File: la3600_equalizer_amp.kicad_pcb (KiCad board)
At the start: 2 copper layers, 95 x 198.6 mm, 54 parts, among them J1 JACK_TRS_3PINS, J2 JACK_TRS_3PINS, J3 USB_B, U1 LA3600, U2 LA3600, U3 LM386, U4 LM386

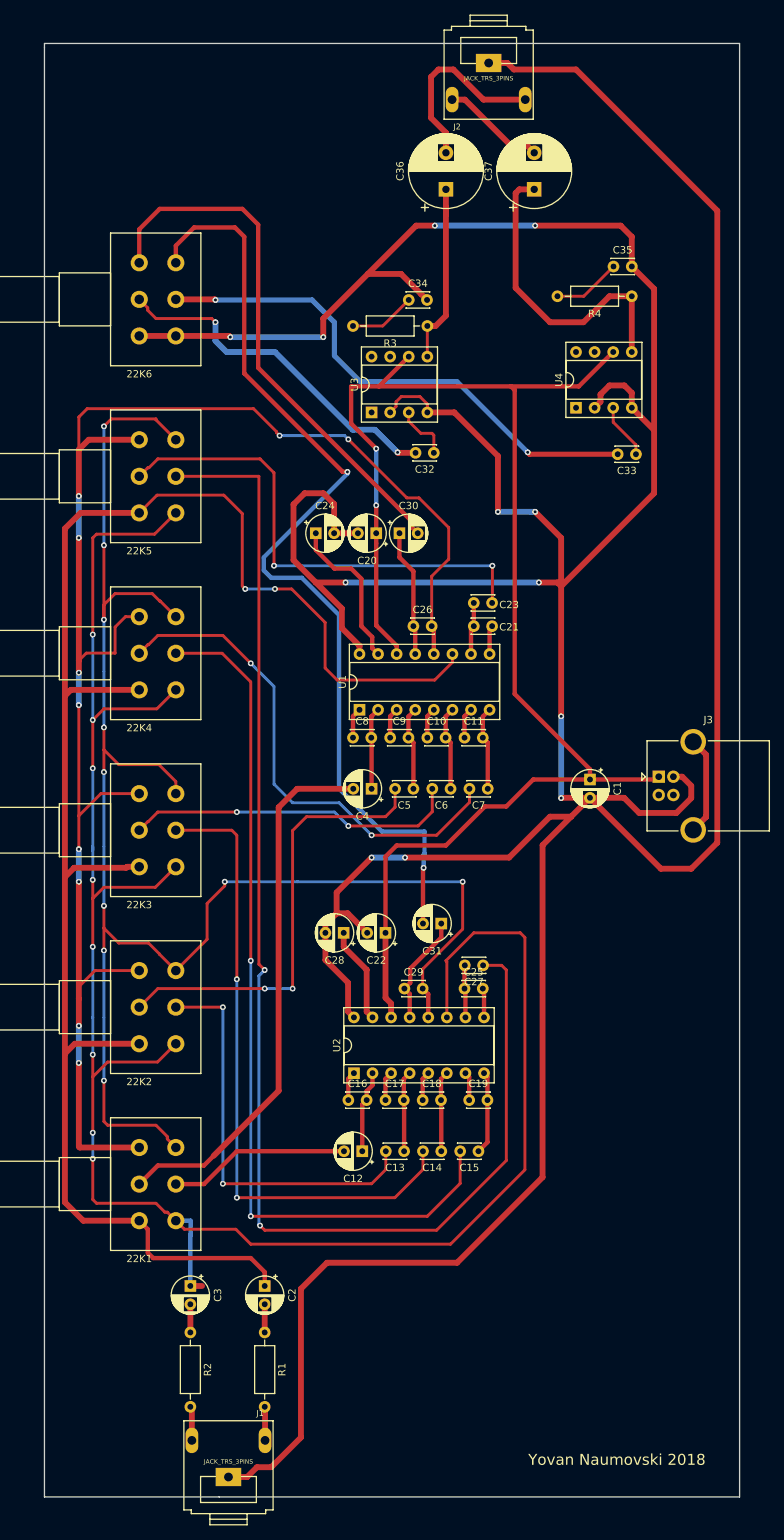
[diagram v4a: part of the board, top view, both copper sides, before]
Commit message: replace the audio amplifier part of the circuit with a new one based on NE5532 and BD139/BD140 output stage
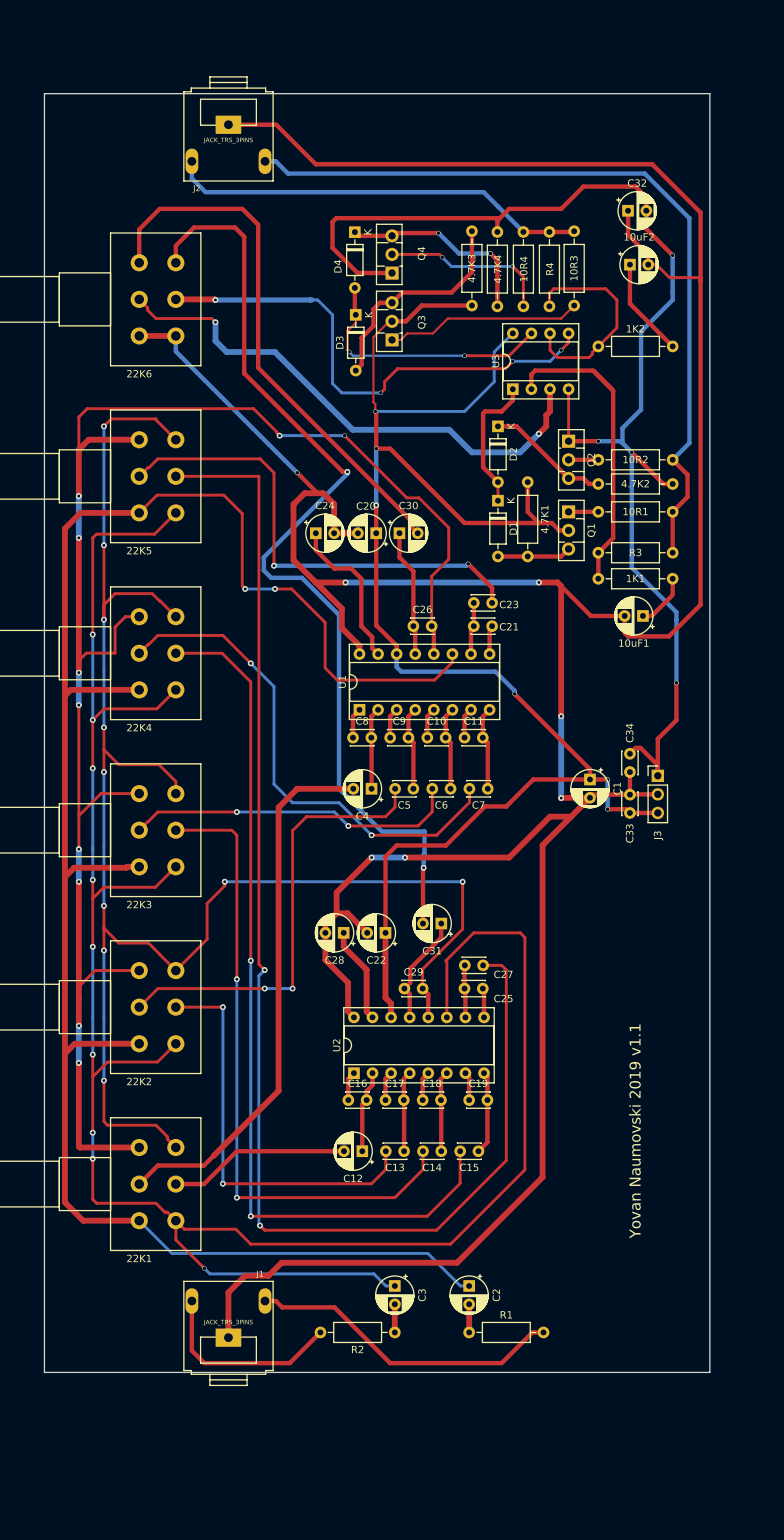
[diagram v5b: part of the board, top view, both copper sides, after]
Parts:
- removed C35: 47nF, Capacitor_THT:C_Disc_D3.0mm_W2.0mm_P2.50mm
- removed C36, C37: 1000uF, Capacitor_THT:CP_Radial_D10.0mm_P5.00mm
- removed U4: LM386, Package_DIP:DIP-8_W7.62mm_Socket
- added 10R1: 10R, Resistor_THT:R_Axial_DIN0207_L6.3mm_D2.5mm_P10.16mm_Horizontal, F.Cu at (99.6, 81.8)
- added 10R2: 10R, Resistor_THT:R_Axial_DIN0207_L6.3mm_D2.5mm_P10.16mm_Horizontal, F.Cu at (109.7, 74.7)
- added 10R3: 10R, Resistor_THT:R_Axial_DIN0207_L6.3mm_D2.5mm_P10.16mm_Horizontal, F.Cu at (96.3, 53.6)
- added 10R4: 10R, Resistor_THT:R_Axial_DIN0207_L6.3mm_D2.5mm_P10.16mm_Horizontal, F.Cu at (89.3, 43.5)
- added 10uF1: 10uF, Capacitor_THT:CP_Radial_D5.0mm_P2.50mm, F.Cu at (105.7, 96.0)
- added 10uF2: 10uF, Capacitor_THT:CP_Radial_D5.0mm_P2.50mm, F.Cu at (103.9, 48.0)
- added 1K1: 1K, Resistor_THT:R_Axial_DIN0207_L6.3mm_D2.5mm_P10.16mm_Horizontal, F.Cu at (99.6, 90.9)
- added 1K2: 1K, Resistor_THT:R_Axial_DIN0207_L6.3mm_D2.5mm_P10.16mm_Horizontal, F.Cu at (99.6, 59.2)
- added 4.7K1: 4.7K, Resistor_THT:R_Axial_DIN0207_L6.3mm_D2.5mm_P10.16mm_Horizontal, F.Cu at (89.9, 77.7)
- added 4.7K2: 4.7K, Resistor_THT:R_Axial_DIN0207_L6.3mm_D2.5mm_P10.16mm_Horizontal, F.Cu at (99.6, 78.0)
- added 4.7K3: 4.7K, Resistor_THT:R_Axial_DIN0207_L6.3mm_D2.5mm_P10.16mm_Horizontal, F.Cu at (82.3, 53.6)
- added 4.7K4: 4.7K, Resistor_THT:R_Axial_DIN0207_L6.3mm_D2.5mm_P10.16mm_Horizontal, F.Cu at (85.8, 53.7)
- added D1: 1N4148, Diode_THT:D_DO-35_SOD27_P7.62mm_Horizontal, F.Cu at (85.9, 80.3)
- added D2: 1N4148, Diode_THT:D_DO-35_SOD27_P7.62mm_Horizontal, F.Cu at (85.9, 70.1)
- added D3: 1N4148, Diode_THT:D_DO-35_SOD27_P7.62mm_Horizontal, F.Cu at (66.4, 54.9)
- added D4: 1N4148, Diode_THT:D_DO-35_SOD27_P7.62mm_Horizontal, F.Cu at (66.3, 43.6)
- added Q1: BD139, Package_TO_SOT_THT:TO-126-3_Vertical, F.Cu at (95.5, 81.8)
- added Q2: BD140, Package_TO_SOT_THT:TO-126-3_Vertical, F.Cu at (95.5, 72.1)
- added Q3: BD139, Package_TO_SOT_THT:TO-126-3_Vertical, F.Cu at (71.4, 58.3)
- added Q4: BD140, Package_TO_SOT_THT:TO-126-3_Vertical, F.Cu at (71.4, 49.1)
- C32: value 100nF -> 100uF; footprint Capacitor_THT:C_Disc_D3.0mm_W2.0mm_P2.50mm -> Capacitor_THT:CP_Radial_D5.0mm_P2.50mm
- C34: value 47nF -> 100nF
- J3: value USB_B -> Conn_01x03; footprint Connector_USB:USB_B_OST_USB-B1HSxx_Horizontal -> Connector_PinHeader_2.54mm:PinHeader_1x03_P2.54mm_Vertical
- R3, R4: value 10 -> 10K
- U3: value LM386 -> NE5532
- moved C34 71.2 mm to (103.9, 117.3), turned to 90 degrees
- moved C33 49.0 mm to (103.9, 122.9), turned to 90 degrees
- moved R3 45.7 mm to (109.7, 87.4)
- moved C32 42.4 mm to (103.6, 40.6), turned to 0 degrees
- moved J2 36.5 mm to (49.0, 30.5)
- moved C2 27.9 mm to (81.9, 187.6)
- moved R1 27.9 mm to (81.9, 193.9), turned to 0 degrees
- moved C3 27.9 mm to (71.8, 187.6)
- moved R2 27.9 mm to (71.8, 193.9), turned to 180 degrees
- moved U3 19.6 mm to (87.9, 65.0)
- moved J1 19.1 mm to (49.0, 193.0)
- moved R4 14.3 mm to (92.9, 43.5), turned to 270 degrees
- moved J3 0.18 mm to (107.7, 117.9)
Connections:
- C1 pad 1: Vcc -> +9V
- C20 pad 1: Vcc -> +9V
- C22 pad 1: Vcc -> +9V
- C32 pad 1: Net-(C32-Pad1) -> GND
- C32 pad 2: Net-(22K6-Pad2) -> -9V
- C33 pad 1: Net-(C33-Pad1) -> +9V
- C33 pad 2: Net-(22K6-Pad5) -> GND
- C34 pad 1: Net-(C34-Pad1) -> GND
- C34 pad 2: GND -> -9V
- J2 pad 2: Net-(C36-Pad2) -> Net-(10R1-Pad2)
- J2 pad 3: Net-(C37-Pad2) -> Net-(10R3-Pad2)
- J3 pad 1: Vcc -> -9V
- J3 pad 2: Net-(J3-Pad2) -> GND
- J3 pad 3: Net-(J3-Pad3) -> +9V
- R3 pad 1: Net-(C36-Pad1) -> Net-(10R1-Pad2)
- R3 pad 2: Net-(C34-Pad1) -> Net-(1K1-Pad1)
- R4 pad 1: Net-(C37-Pad1) -> Net-(10R3-Pad2)
- R4 pad 2: Net-(C35-Pad1) -> Net-(1K2-Pad1)
- U1 pad 14: Vcc -> +9V
- U2 pad 14: Vcc -> +9V
- U3 pad 2: GND -> Net-(1K1-Pad1)
- U3 pad 3: Net-(C32-Pad1) -> Net-(22K6-Pad2)
- U3 pad 4: GND -> -9V
- U3 pad 5: Net-(C36-Pad1) -> Net-(22K6-Pad5)
- U3 pad 6: Vcc -> Net-(1K2-Pad1)
- U3 pad 8: Net-(U3-Pad8) -> +9V
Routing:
- net +9V: track 0.00 -> 237.0 mm, vias 0 -> 6
- net Vcc: track 205.0 -> 0.00 mm, vias 2 -> 0
- net -9V: track 0.00 -> 176.6 mm, vias 0 -> 4
- net GND: track 658.9 -> 488.8 mm, vias 12 -> 7
- net Net-(10R1-Pad2): track 0.00 -> 109.6 mm
- net Net-(10R3-Pad2): track 0.00 -> 57.7 mm
- net Net-(1K1-Pad1): track 0.00 -> 52.8 mm
- net Net-(C37-Pad1): track 42.6 -> 0.00 mm
- net Net-(J1-Pad3): track 4.61 -> 43.3 mm
- net Net-(D3-Pad1): track 0.00 -> 35.8 mm, vias 0 -> 2
- net Net-(4.7K3-Pad2): track 0.00 -> 30.5 mm
- net Net-(1K2-Pad1): track 0.00 -> 29.4 mm
- net Net-(4.7K4-Pad1): track 0.00 -> 27.7 mm, vias 0 -> 2
- net Net-(10R3-Pad1): track 0.00 -> 26.8 mm
- net Net-(C36-Pad2): track 26.2 -> 0.00 mm
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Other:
- board size 95 x 198.6 mm -> 90.9 x 174.8 mm
- board text added: "Yovan Naumovski 2019 v1.1"
- board text removed: "Yovan Naumovski 2018"
